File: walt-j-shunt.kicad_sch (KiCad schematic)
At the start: 15 parts, among them J1 Screw_Terminal_01x03

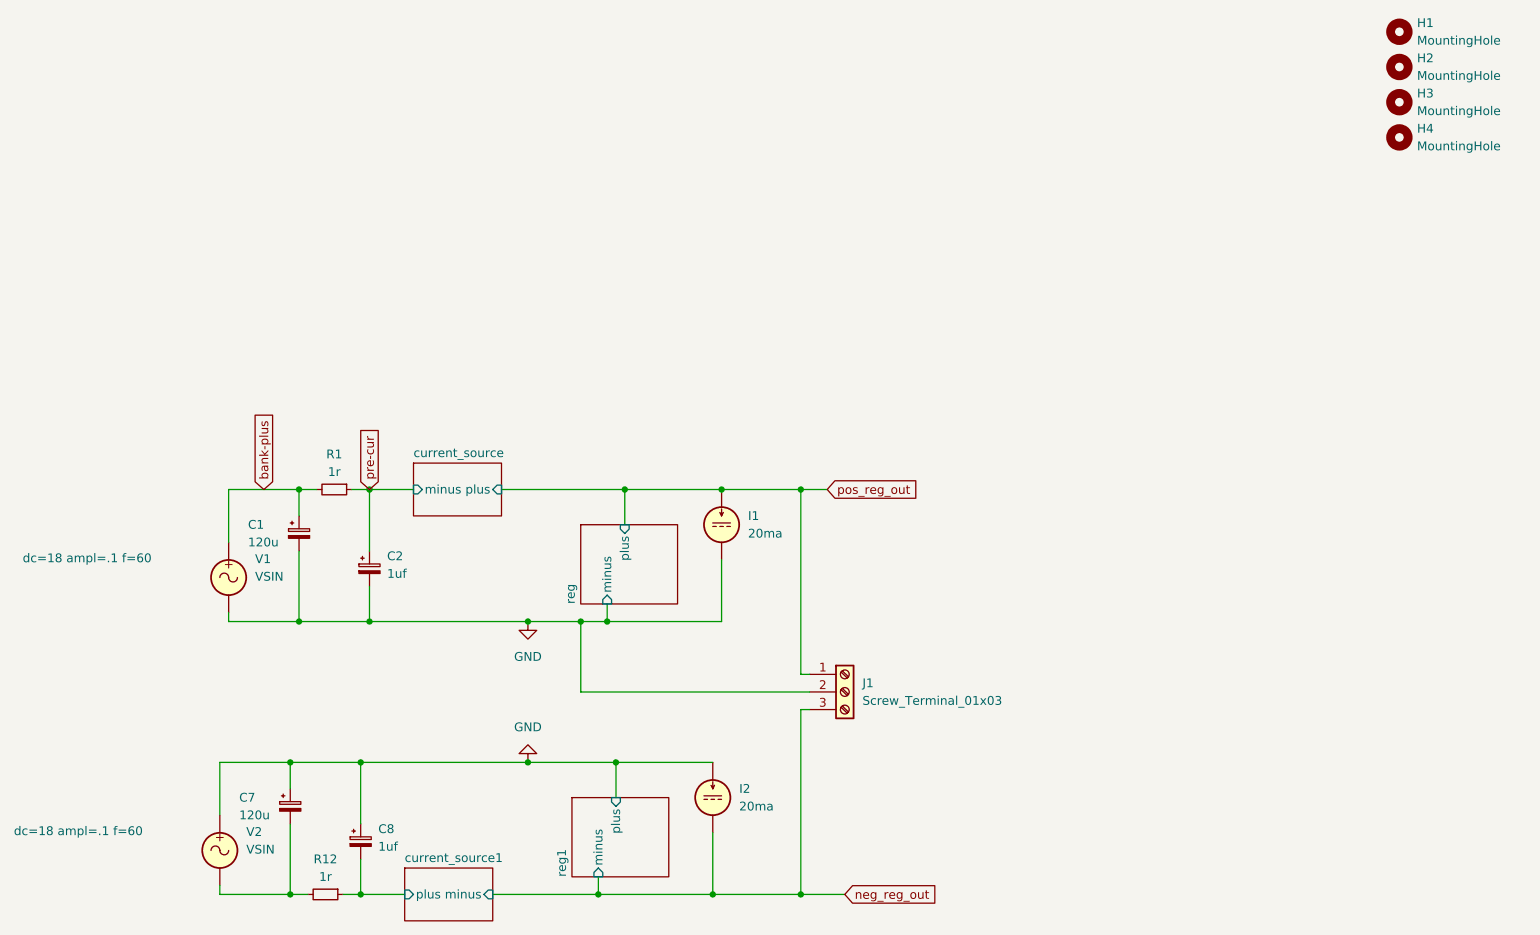
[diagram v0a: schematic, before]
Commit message: Current design with SMD MOSFET (before switching to THT)
🤖 Generated with [Claude Code](https://claude.ai/code)

Co-Authored-By: Claude <noreply@anthropic.com>
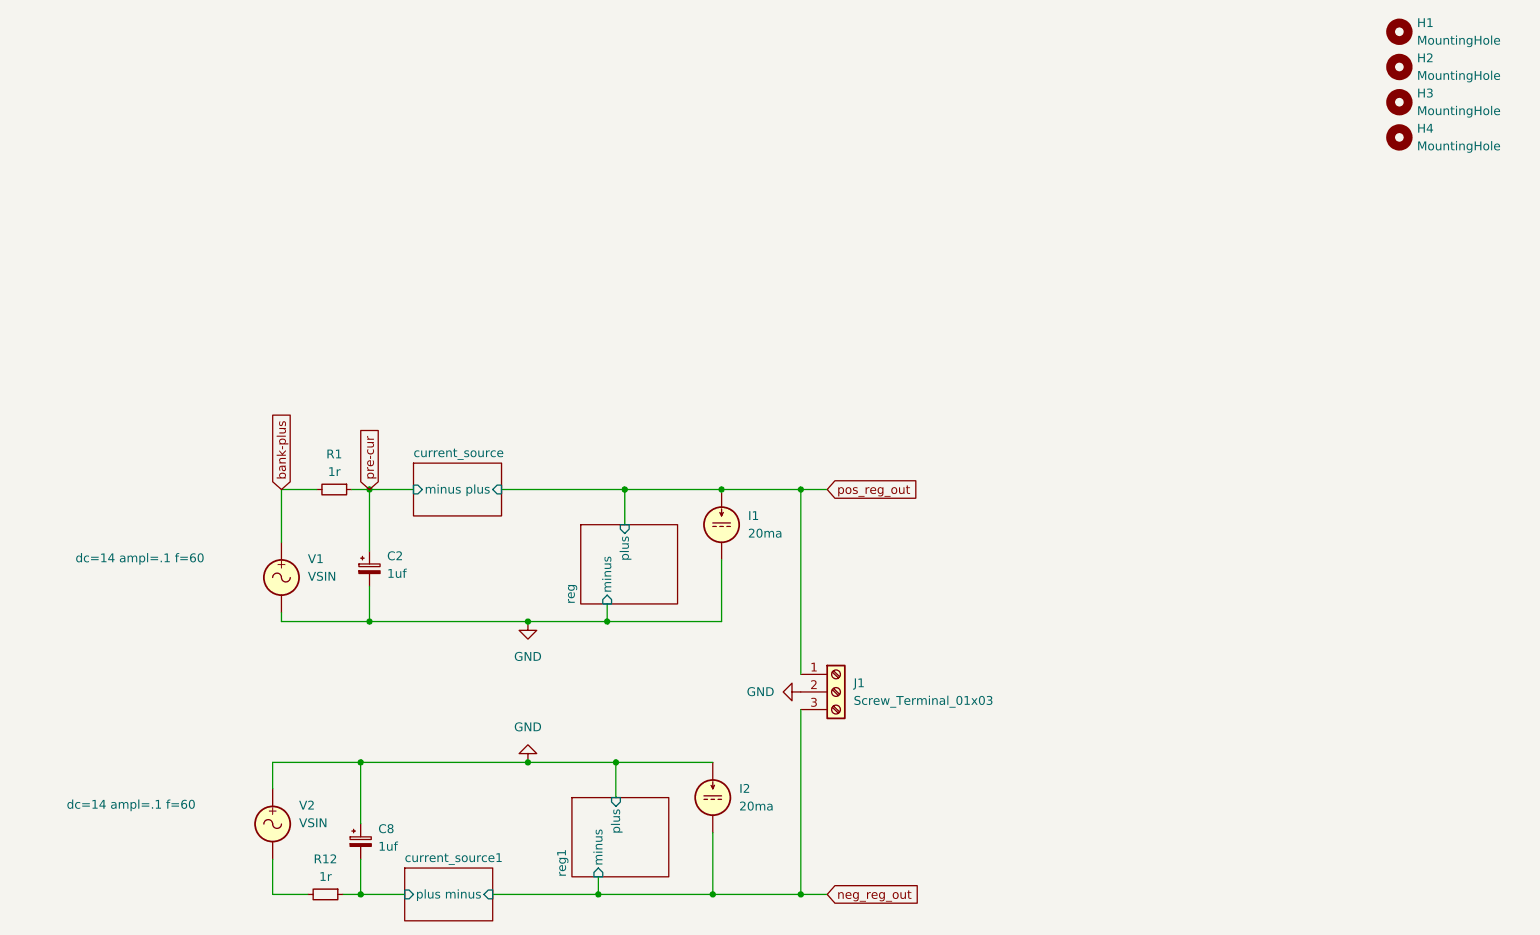
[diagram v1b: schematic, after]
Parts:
- removed C1, C7: 120u, Capacitor_THT:CP_Radial_D5.0mm_P2.00mm, symbol Device:C_Polarized_Small
- J1: footprint TerminalBlock_Altech:Altech_AK100_1x03_P5.00mm -> Connector_Molex:Molex_KK-254_AE-6410-03A_1x03_P2.54mm_Vertical
- R1, R12: footprint Resistor_SMD:R_1206_3216Metric -> Resistor_SMD:R_0805_2012Metric
- V1, V2: footprint Samacsys:395443002 -> Connector_Molex:Molex_KK-254_AE-6410-02A_1x02_P2.54mm_Vertical
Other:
- moved on the sheet: V1, V2

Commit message: Single rail design - initial branch
🤖 Generated with [Claude Code](https://claude.ai/code)

Co-Authored-By: Claude <noreply@anthropic.com>
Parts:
- removed C8: 1uf, Samacsys:B32529C105J, symbol Device:C_Polarized_Small
- removed I2: 20ma, Samacsys:395443002, symbol Simulation_SPICE:IDC
- removed R12: 1r, Resistor_SMD:R_0805_2012Metric, symbol Device:R_Small
- removed V2: VSIN, Connector_Molex:Molex_KK-254_AE-6410-02A_1x02_P2.54mm_Vertical, symbol Simulation_SPICE:VSIN
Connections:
- net neg_reg_out: no longer names the net of J1.3 (Pin_3)
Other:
- removed sheet current_source1
- removed sheet reg1
- sheet current_source ports: added +, -; removed minus, plus
- sheet reg ports: added +, -; removed minus, plus
- moved on the sheet: C2, I1, J1, R1, V1
